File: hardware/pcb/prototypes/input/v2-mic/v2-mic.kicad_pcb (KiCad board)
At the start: 2 copper layers, 66 x 43.8 mm, 56 parts, among them J1 TRS, J10 Conn_01x02_Pin, J11 XLR, J3 Conn_01x03_Pin, J4 Conn_01x05_Pin, J5 Conn_01x09_Pin, J6 PH_EN, J7 Conn_01x06_Pin, J8 Conn_01x08_Pin, J9 OUT_BIAS, U1 THAT5263, U2 THAT1580, U3 OPA1637

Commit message: add label and aisler logo
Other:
- board text added: "OpenMic Mic input v0.2 7/16/26"
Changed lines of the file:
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@@
+	)
+	(gr_rect
+		(start 100.302 35.814)
+		(end 130.302 43.314)
+		(stroke
+			(width 0.08382)
+			(type default)
+		)
+		(fill no)
+		(layer "B.SilkS")
 	)
 	(gr_rect
@@
 		)
 	)
+	(gr_text "OpenMic\nMic input v0.2\n7/16/26"
+		(at 163.83 41.656 -0)
+		(layer "B.SilkS")
+		(effects
+			(font
+				(size 1.5 1.5)
+				(thickness 0.3)
+				(bold yes)
+			)
+			(justify left bottom mirror)
+		)
+	)

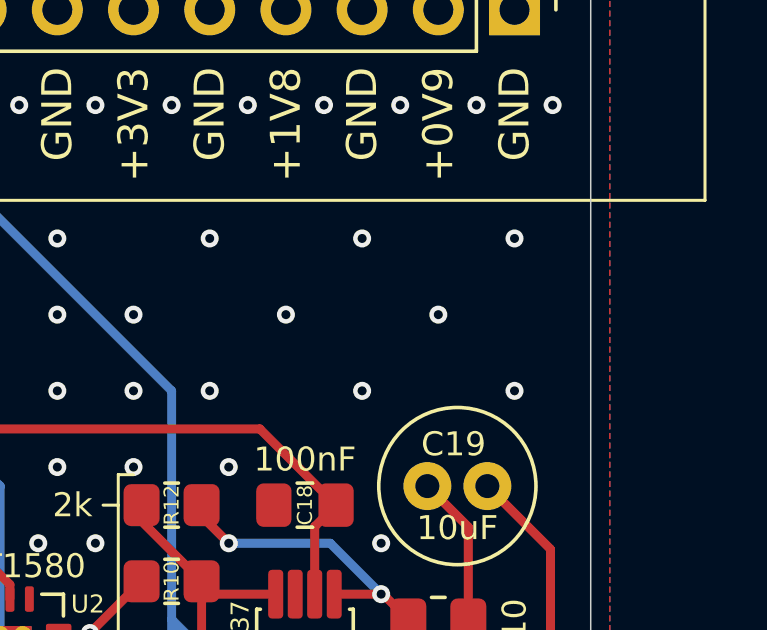
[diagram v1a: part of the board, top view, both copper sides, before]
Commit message: add exposed gnd pins
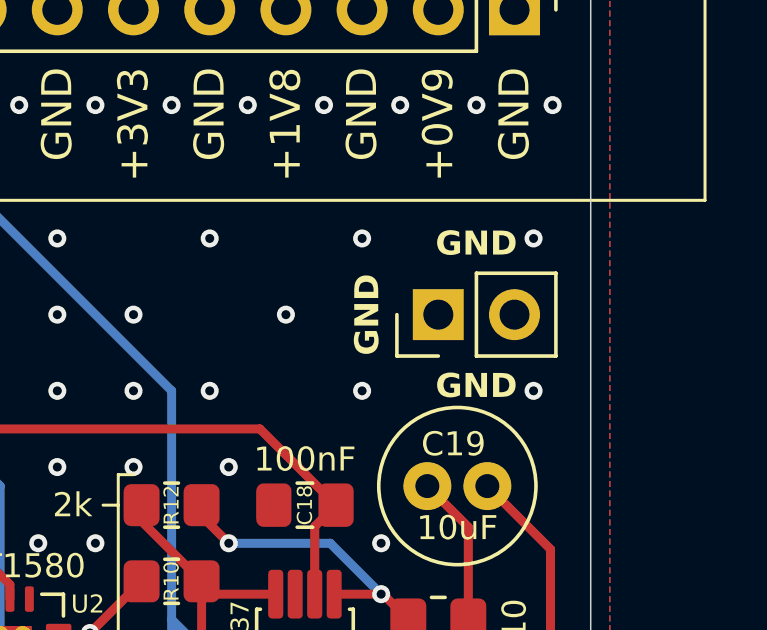
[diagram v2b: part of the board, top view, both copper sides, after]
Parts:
- added J2: Conn_01x02_Pin, Connector_PinHeader_2.54mm:PinHeader_1x02_P2.54mm_Vertical, F.Cu at (160.0, 43.2)
